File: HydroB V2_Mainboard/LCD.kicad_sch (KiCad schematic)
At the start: 0 parts

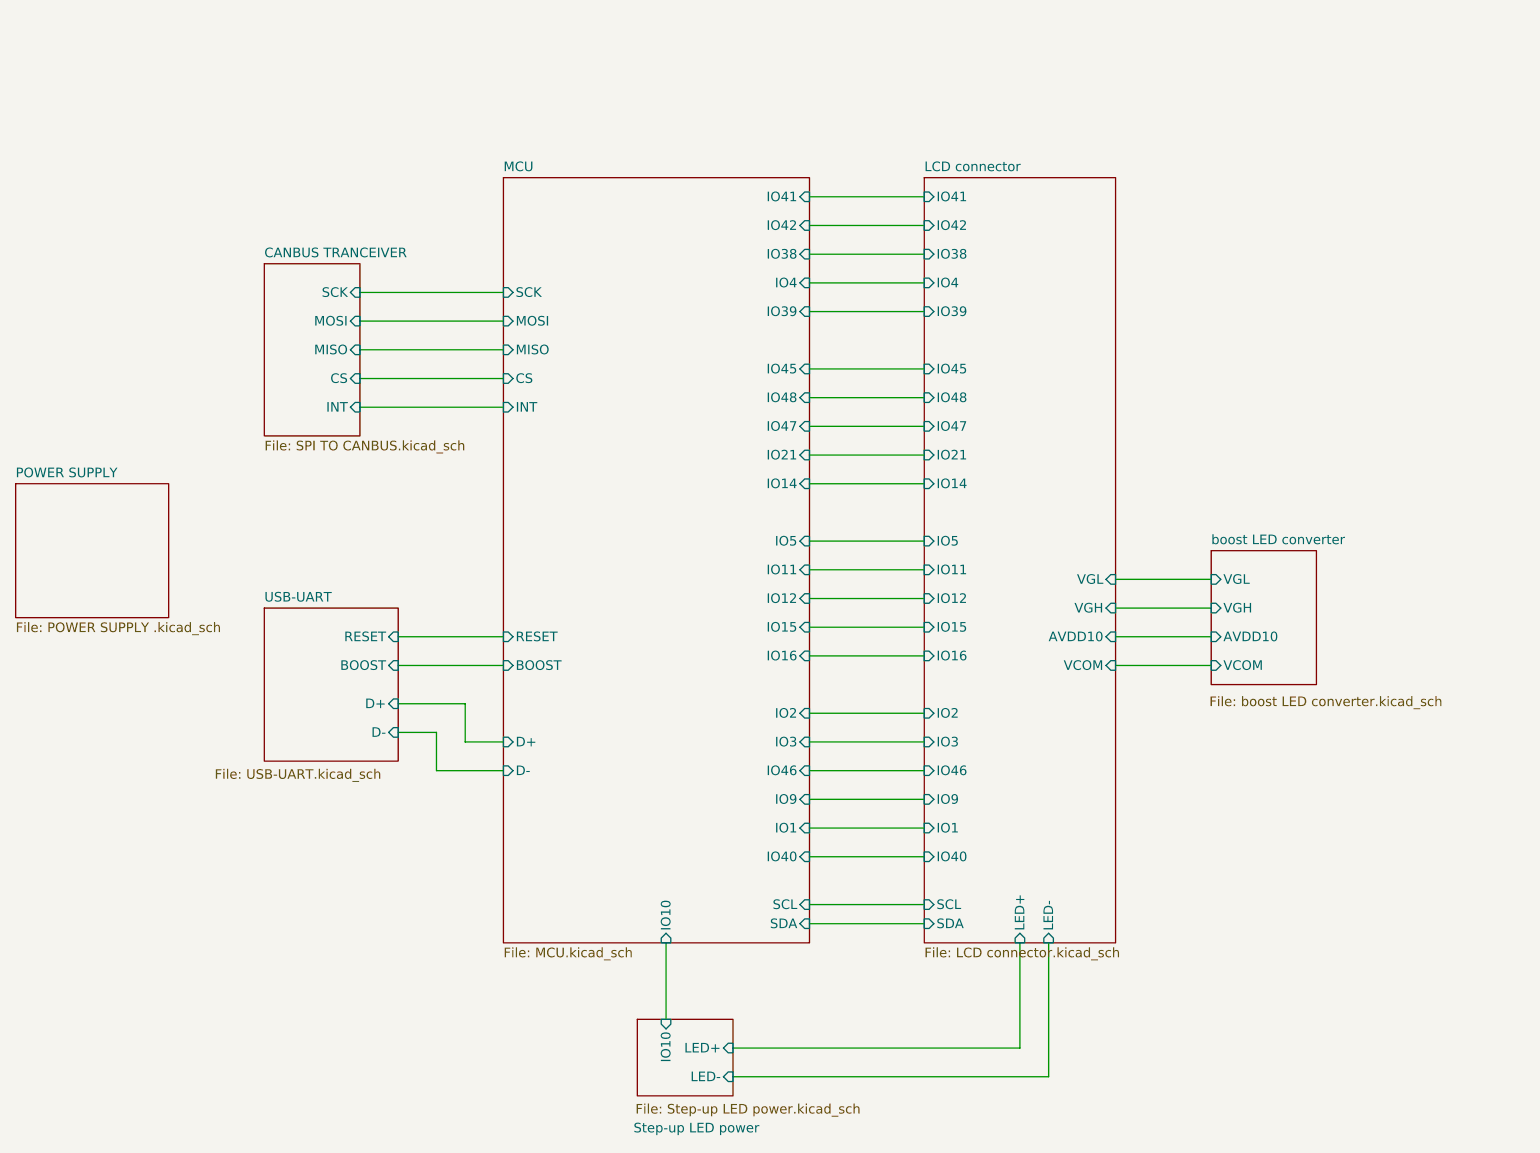
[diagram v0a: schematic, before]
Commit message: Update LCD schematic
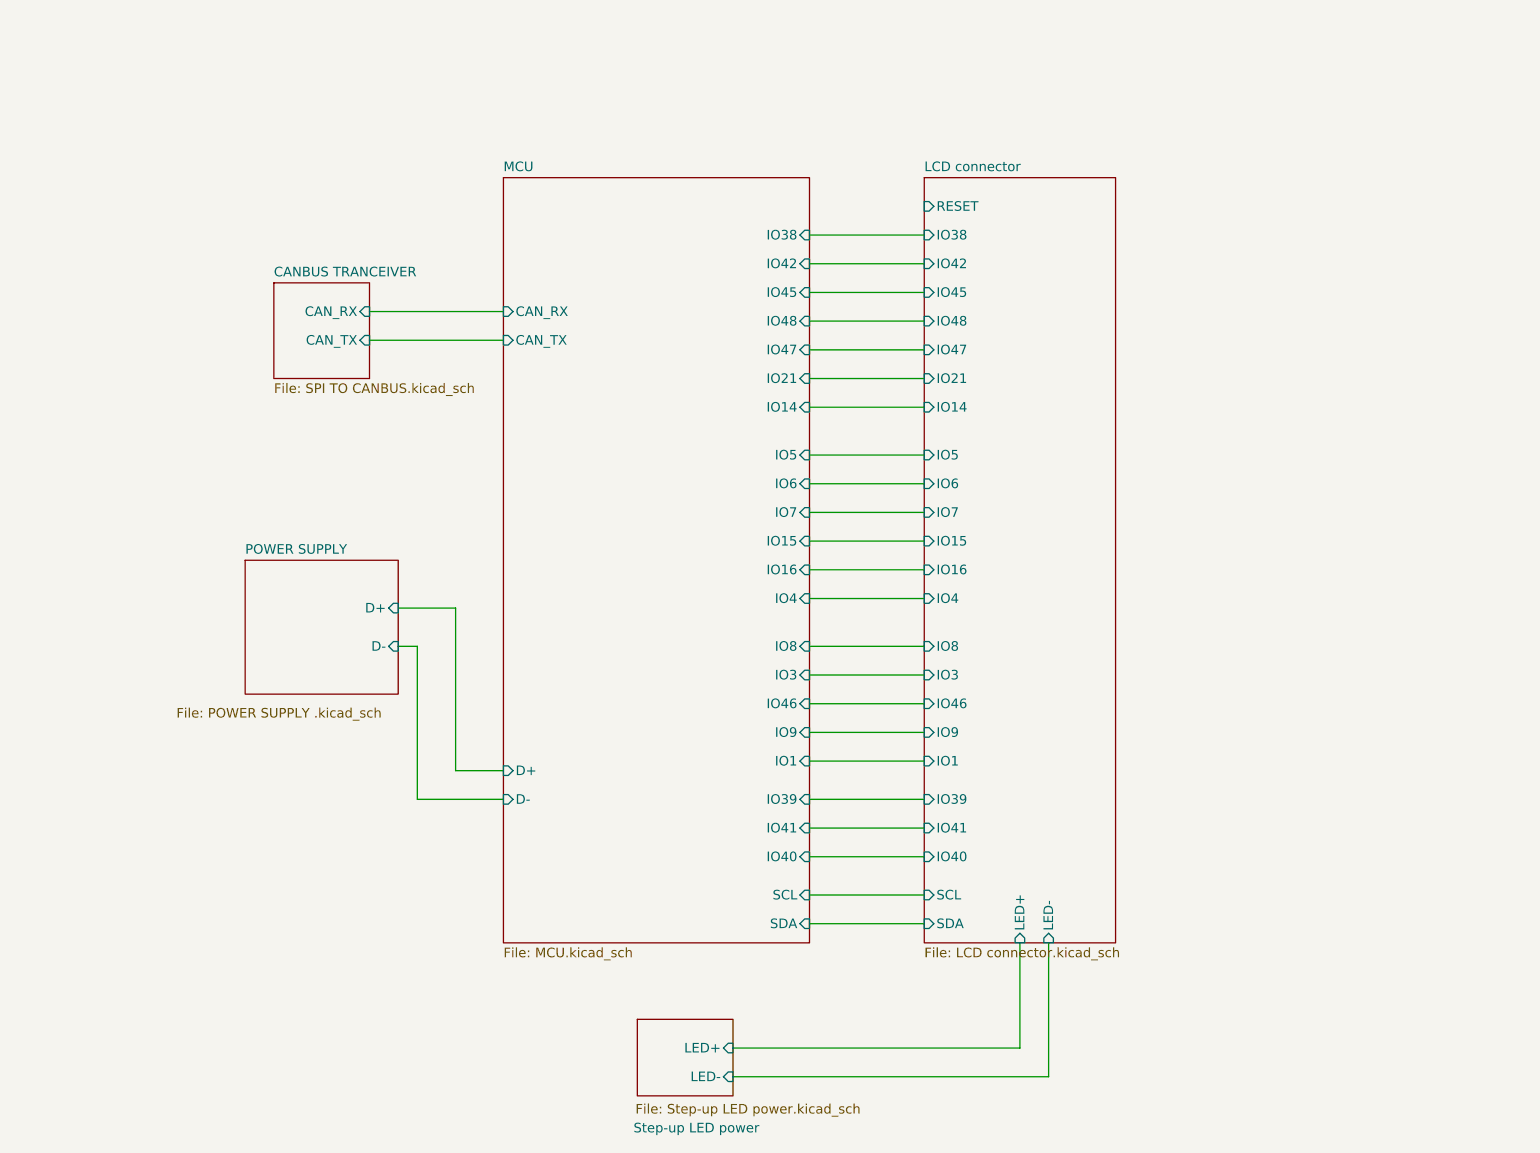
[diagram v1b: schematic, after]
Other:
- removed sheet USB-UART
- removed sheet boost LED converter
- sheet CANBUS TRANCEIVER ports: added CAN_RX, CAN_TX; removed CS, INT, MISO, MOSI, SCK
- sheet LCD connector ports: added IO6, IO7, IO8, RESET; removed AVDD10, IO11, IO12, IO2, VCOM, VGH, VGL
- sheet MCU ports: added CAN_RX, CAN_TX, IO6, IO7, IO8; removed BOOST, CS, INT, IO10, IO11, IO12, IO2, MISO, MOSI, RESET, SCK
- sheet POWER SUPPLY  ports: added D+, D-; removed none
- sheet Step-up LED power ports: added none; removed IO10

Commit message: mainboard updated
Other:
- sheet MCU ports: added IO35; removed none
- sheet Step-up LED power ports: added IO35; removed none
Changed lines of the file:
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@@
+	(wire
+		(pts
+			(xy 134.62 144.78) (xy 134.62 154.94)
+		)
+		(stroke
+			(width 0)
+			(type default)
+		)
+	)
 	(wire
 		(pts
@@
 			)
 		)
+		(pin "IO35" input
+			(at 134.62 144.78 270)
+			(effects
+				(font
+					(size 1.27 1.27)
+				)
+				(justify left)
+			)
+		)
 		(instances
 			(project "LCD High Revolution"
@@
 			(effects
 				(font
+					(size 1.27 1.27)
+				)
+				(justify right)
+			)
+		)
+		(pin "IO35" input
+			(at 134.62 154.94 90)
+			(effects
+				(font

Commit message: Schematic mainboard update
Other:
- removed sheet CANBUS TRANCEIVER
- added sheet High speed  (High speed.kicad_sch)
- added sheet Modbus (untitled.kicad_sch)
- sheet LCD connector ports: added B3, B4, B5, B6, B7, G2, G3, G4, G5, G6, G7, HSYNC, INT, LCD_DE, LCD_PCLK, R3, R4, R5, R6, R7, RST, VSYNC; removed IO1, IO14, IO15, IO16, IO21, IO3, IO38, IO39, IO4, IO40, IO41, IO42, IO45, IO46, IO47, IO48, IO5, IO6, IO7, IO8, IO9, RESET
- sheet MCU ports: added B3, B4, B5, B6, B7, BL_PWM, BUSY, EN_RS485, G2, G3, G4, G5, G6, G7, HSYNC, INT, LCD DE, LCD_PCLK, R3, R4, R5, R6, R7, RS485_RX, RS485_TX, RST, RX, TX, VSYNC; removed CAN_RX, CAN_TX, IO1, IO14, IO15, IO16, IO21, IO3, IO35, IO38, IO39, IO4, IO40, IO41, IO42, IO45, IO46, IO47, IO48, IO5, IO6, IO7, IO8, IO9
- sheet Step-up LED power ports: added BL_PWM; removed IO35
